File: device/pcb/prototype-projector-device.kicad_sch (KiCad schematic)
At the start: 22 parts, among them J1 LED, J2 Serial-UPDI, J3 UART, J4 DMX1, J5 DMX2, U1 ATtiny202-SS, U2 NJM78L33SU3, U3 CL6808, U4 MAX3485

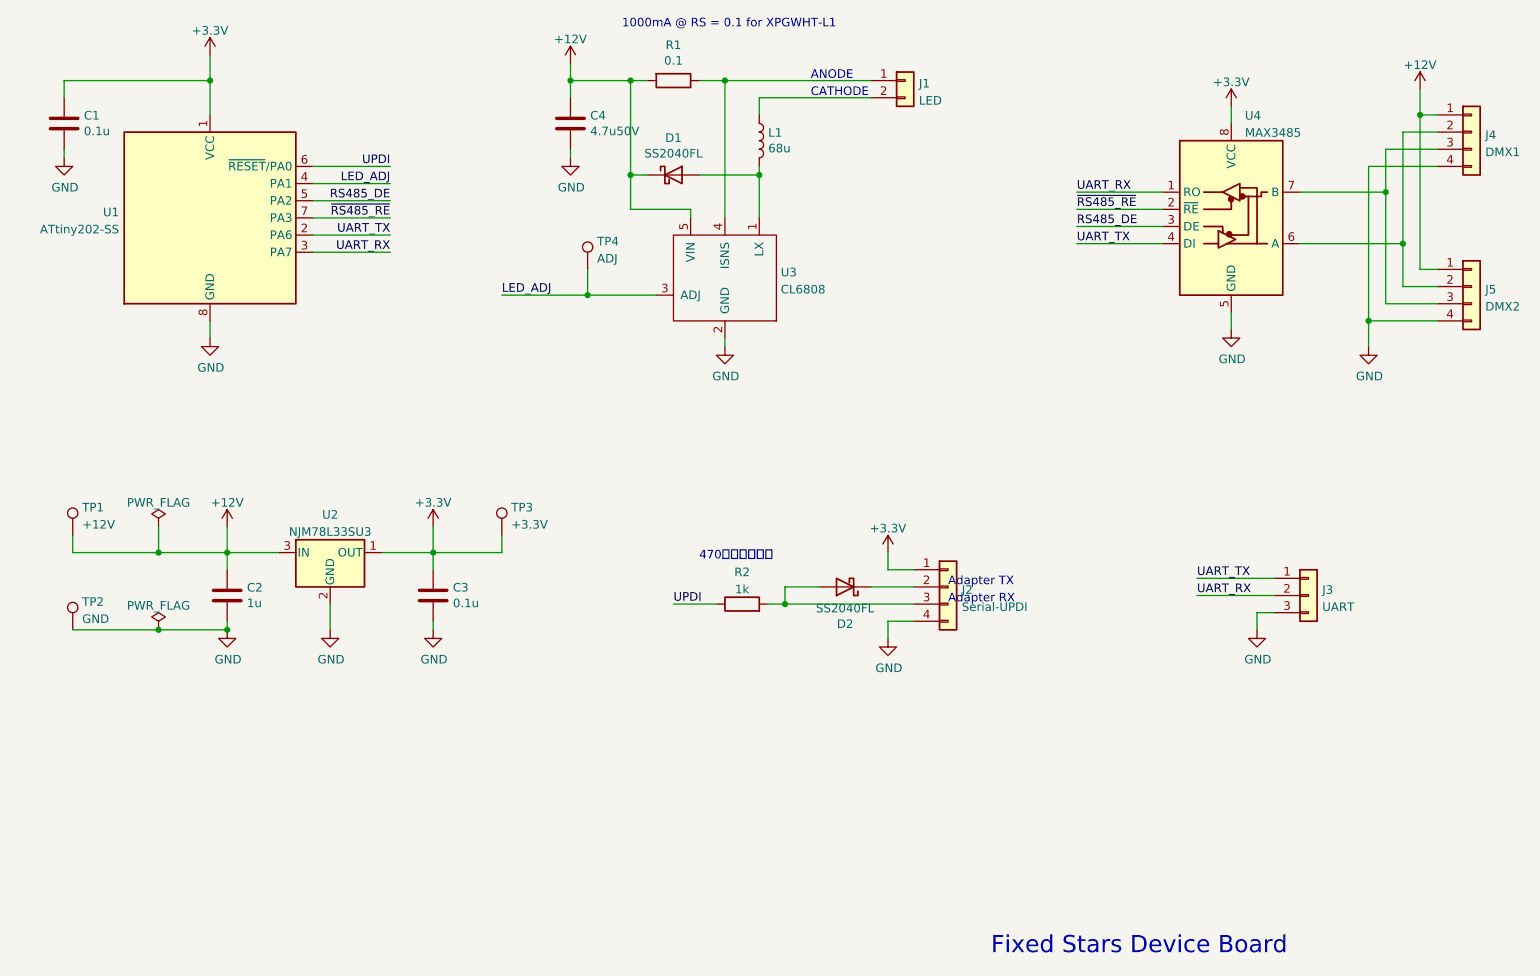
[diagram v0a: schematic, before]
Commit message: modify: 24V駆動対応 v0.1.1
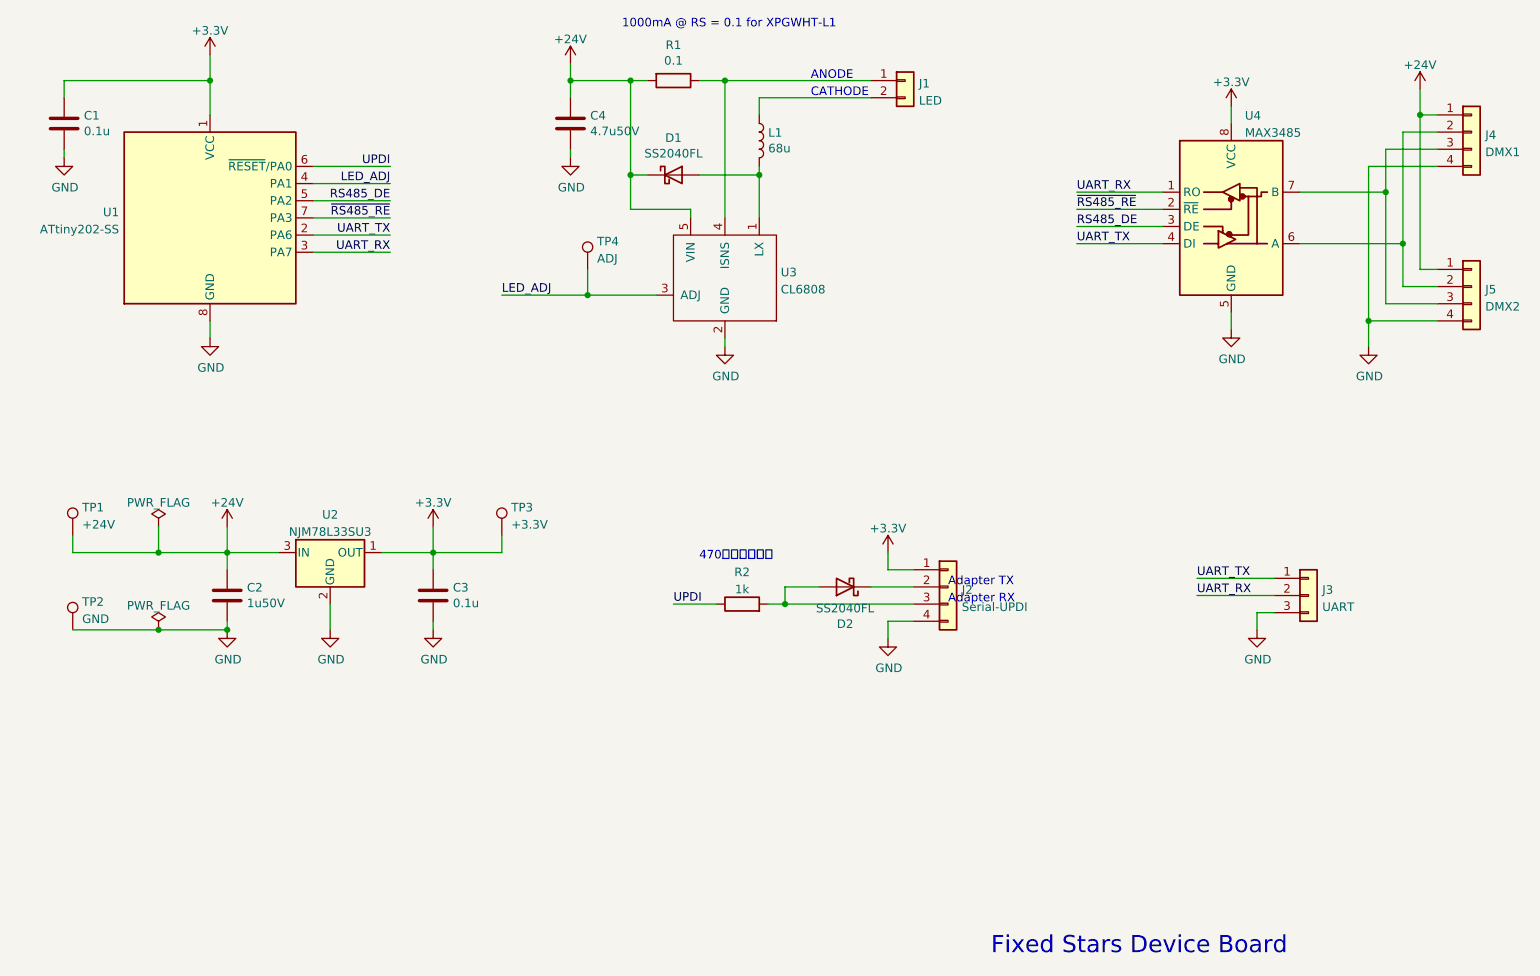
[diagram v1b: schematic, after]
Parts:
- C2: value 1u -> 1u50V
- TP1: value +12V -> +24V
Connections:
- net +12V renamed +24V
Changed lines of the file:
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@@
     (pin "2")
+  )
+  (symbol (lib_id "power:+24V") (at 118.11 44.45 0) (unit 1)
+    (in_bom yes) (on_board yes) (fields_autoplaced)
+    (property "Reference" "#PWR0101" (id 0) (at 118.11 48.26 0)
+      (effects (font (size 1.27 1.27)) hide)
+    )
+    (property "Value" "+24V" (id 1) (at 118.11 40.8742 0))
+    (property "Footprint" "" (id 2) (at 118.11 44.45 0)
+      (effects (font (size 1.27 1.27)) hide)
+    )
+    (property "Datasheet" "" (id 3) (at 118.11 44.45 0)
+      (effects (font (size 1.27 1.27)) hide)
+    )
+    (pin "1")
   )
   (symbol (lib_id "power:GND") (at 97.79 128.27 0) (unit 1)
@@
     (pin "1")
   )
-  (symbol (lib_id "power:+12V") (at 243.84 48.26 0) (unit 1)
-    (in_bom yes) (on_board yes) (fields_autoplaced)
-    (property "Reference" "#PWR018" (id 0) (at 243.84 52.07 0)
-      (effects (font (size 1.27 1.27)) hide)
-    )
-    (property "Value" "+12V" (id 1) (at 243.84 44.6842 0))
-    (property "Footprint" "" (id 2) (at 243.84 48.26 0)
-      (effects (font (size 1.27 1.27)) hide)
-    )
-    (property "Datasheet" "" (id 3) (at 243.84 48.26 0)
-      (effects (font (size 1.27 1.27)) hide)
-    )
-    (pin "1")
-  )
   (symbol (lib_id "power:GND") (at 43.18 58.42 0) (unit 1)
     (in_bom yes) (on_board yes)
@@
       (effects (font (size 1.27 1.27)) (justify left))
     )
-    (property "Value" "+12V" (id 1) (at 45.847 112.7002 0)
+    (property "Value" "+24V" (id 1) (at 45.847 112.7002 0)
       (effects (font (size 1.27 1.27)) (justify left))
     )
@@
     )
     (property "Datasheet" "~" (id 3) (at 49.53 114.3 0)
-      (effects (font (size 1.27 1.27)) hide)
-    )
-    (pin "1")
-  )
-  (symbol (lib_id "power:+12V") (at 118.11 44.45 0) (unit 1)
-    (in_bom yes) (on_board yes) (fields_autoplaced)
-    (property "Reference" "#PWR09" (id 0) (at 118.11 48.26 0)
-      (effects (font (size 1.27 1.27)) hide)
-    )
-    (property "Value" "+12V" (id 1) (at 118.11 40.8742 0))
-    (property "Footprint" "" (id 2) (at 118.11 44.45 0)
-      (effects (font (size 1.27 1.27)) hide)
-    )
-    (property "Datasheet" "" (id 3) (at 118.11 44.45 0)
       (effects (font (size 1.27 1.27)) hide)
     )
@@
     (pin "1")
   )
-  (symbol (lib_id "power:+12V") (at 67.31 113.03 0) (unit 1)
-    (in_bom yes) (on_board yes)
-    (property "Reference" "#PWR04" (id 0) (at 67.31 116.84 0)
-      (effects (font (size 1.27 1.27)) hide)
-    )
-    (property "Value" "+12V" (id 1) (at 67.31 109.4542 0))
+  (symbol (lib_id "power:+24V") (at 243.84 48.26 0) (unit 1)
+    (in_bom yes) (on_board yes) (fields_autoplaced)
+    (property "Reference" "#PWR0102" (id 0) (at 243.84 52.07 0)
+      (effects (font (size 1.27 1.27)) hide)
+    )
+    (property "Value" "+24V" (id 1) (at 243.84 44.6842 0))
+    (property "Footprint" "" (id 2) (at 243.84 48.26 0)
+      (effects (font (size 1.27 1.27)) hide)
+    )
+    (property "Datasheet" "" (id 3) (at 243.84 48.26 0)
+      (effects (font (size 1.27 1.27)) hide)
+    )
+    (pin "1")
+  )
+  (symbol (lib_id "Device:C") (at 67.31 123.19 0) (unit 1)
+    (in_bom yes) (on_board yes)
+    (property "Reference" "C2" (id 0) (at 70.231 122.0216 0)
+      (effects (font (size 1.27 1.27)) (justify left))
+    )
+    (property "Value" "1u50V" (id 1) (at 70.231 124.333 0)
+      (effects (font (size 1.27 1.27)) (justify left))
+    )
+    (property "Footprint" "Capacitor_SMD:C_0603_1608Metric" (id 2) (at 68.2752 127 0)
+      (effects (font (size 1.27 1.27)) hide)
+    )
+    (property "Datasheet" "https://akizukidenshi.com/catalog/g/gP-15331/" (id 3) (at 67.31 123.19 0)
+      (effects (font (size 1.27 1.27)) hide)
+    )
+    (pin "1")
+    (pin "2")
+  )
+  (symbol (lib_id "Connector_Generic:Conn_01x03") (at 227.33 123.19 0) (unit 1)
+    (in_bom yes) (on_board yes) (fields_autoplaced)
+    (property "Reference" "J3" (id 0) (at 229.362 122.3553 0)
+      (effects (font (size 1.27 1.27)) (justify left))
+    )
+    (property "Value" "UART" (id 1) (at 229.362 124.8922 0)
+      (effects (font (size 1.27 1.27)) (justify left))
+    )
+    (property "Footprint" "Connector_PinHeader_2.54mm:PinHeader_1x03_P2.54mm_Vertical" (id 2) (at 227.33 123.19 0)
+      (effects (font (size 1.27 1.27)) hide)
+    )
+    (property "Datasheet" "~" (id 3) (at 227.33 123.19 0)
+      (effects (font (size 1.27 1.27)) hide)
+    )
+    (pin "1")
+    (pin "2")
+    (pin "3")
+  )
+  (symbol (lib_id "power:+24V") (at 67.31 113.03 0) (unit 1)
+    (in_bom yes) (on_board yes) (fields_autoplaced)
+    (property "Reference" "#PWR0103" (id 0) (at 67.31 116.84 0)
+      (effects (font (size 1.27 1.27)) hide)
+    )
+    (property "Value" "+24V" (id 1) (at 67.31 109.4542 0))
     (property "Footprint" "" (id 2) (at 67.31 113.03 0)
       (effects (font (size 1.27 1.27)) hide)
@@
     )
     (pin "1")
-  )
-  (symbol (lib_id "Device:C") (at 67.31 123.19 0) (unit 1)
-    (in_bom yes) (on_board yes)
-    (property "Reference" "C2" (id 0) (at 70.231 122.0216 0)
-      (effects (font (size 1.27 1.27)) (justify left))
-    )
-    (property "Value" "1u" (id 1) (at 70.231 124.333 0)
-      (effects (font (size 1.27 1.27)) (justify left))
-    )
-    (property "Footprint" "Capacitor_SMD:C_0603_1608Metric" (id 2) (at 68.2752 127 0)
-      (effects (font (size 1.27 1.27)) hide)
-    )
-    (property "Datasheet" "https://akizukidenshi.com/catalog/g/gP-16993/" (id 3) (at 67.31 123.19 0)
-      (effects (font (size 1.27 1.27)) hide)
-    )
-    (pin "1")
-    (pin "2")
-  )
-  (symbol (lib_id "Connector_Generic:Conn_01x03") (at 227.33 123.19 0) (unit 1)
-    (in_bom yes) (on_board yes) (fields_autoplaced)
-    (property "Reference" "J3" (id 0) (at 229.362 122.3553 0)
-      (effects (font (size 1.27 1.27)) (justify left))
-    )
-    (property "Value" "UART" (id 1) (at 229.362 124.8922 0)
-      (effects (font (size 1.27 1.27)) (justify left))
-    )
-    (property "Footprint" "Connector_PinHeader_2.54mm:PinHeader_1x03_P2.54mm_Vertical" (id 2) (at 227.33 123.19 0)
-      (effects (font (size 1.27 1.27)) hide)
-    )
-    (property "Datasheet" "~" (id 3) (at 227.33 123.19 0)
-      (effects (font (size 1.27 1.27)) hide)
-    )
-    (pin "1")
-    (pin "2")
-    (pin "3")
   )
   (symbol (lib_id "Device:C") (at 97.79 123.19 0) (unit 1)
@@
       (reference "#PWR03") (unit 1) (value "GND") (footprint "")
     )
-    (path "/ccfaba03-96ff-4759-ac10-8499ad037b49"
-      (reference "#PWR04") (unit 1) (value "+12V") (footprint "")
-    )
     (path "/97dede01-e987-45b8-b767-f5c2b60da356"
       (reference "#PWR05") (unit 1) (value "GND") (footprint "")
@@
       (reference "#PWR08") (unit 1) (value "GND") (footprint "")
     )
-    (path "/a7024ceb-9aa6-44ec-9cc3-6060017540b3"
-      (reference "#PWR09") (unit 1) (value "+12V") (footprint "")
-    )
     (path "/4f84328a-acf9-43ca-9fb6-211ab483adc4"
       (reference "#PWR010") (unit 1) (value "GND") (footprint "")
@@
       (reference "#PWR017") (unit 1) (value "GND") (footprint "")
     )
-    (path "/1c39cee8-2999-48c6-ba34-4b6db5f1e091"
-      (reference "#PWR018") (unit 1) (value "+12V") (footprint "")
+    (path "/0d9deca6-cb27-4133-9530-3b439cf79648"
+      (reference "#PWR0101") (unit 1) (value "+24V") (footprint "")
+    )
+    (path "/c75730b6-b7ac-40cd-b968-25dcd70fe283"
+      (reference "#PWR0102") (unit 1) (value "+24V") (footprint "")
+    )
+    (path "/dffb01eb-3d82-49af-a97e-a460c55974cf"
+      (reference "#PWR0103") (unit 1) (value "+24V") (footprint "")
     )
     (path "/7f8864a4-f5ec-409d-b98e-545e551e51c3"
@@
     )
     (path "/d09047f0-010e-4f5b-8e9a-bae165b62416"
-      (reference "C2") (unit 1) (value "1u") (footprint "Capacitor_SMD:C_0603_1608Metric")
+      (reference "C2") (unit 1) (value "1u50V") (footprint "Capacitor_SMD:C_0603_1608Metric")
     )
     (path "/e9acdb60-f32b-45d4-bc96-0d7838d4b2ad"
@@
     )
     (path "/9b3e521f-dacc-439a-b418-7d1ac6ead2ba"
-      (reference "TP1") (unit 1) (value "+12V") (footprint "TestPoint:TestPoint_THTPad_D2.0mm_Drill1.0mm")
+      (reference "TP1") (unit 1) (value "+24V") (footprint "TestPoint:TestPoint_THTPad_D2.0mm_Drill1.0mm")
     )
     (path "/c7036316-2fd2-4fc4-b239-a2b25e857406"
